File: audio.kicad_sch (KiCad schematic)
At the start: 46 parts, among them J10 NCJ6FA-H-0, J9 NCJ6FA-H-0, Q2 2N3904, Q3 2N3904, Q4 2N3906, Q5 2N3906, U10 OPA1656ID, U11 LM2903, U8 THAT1246, U9 THAT1246

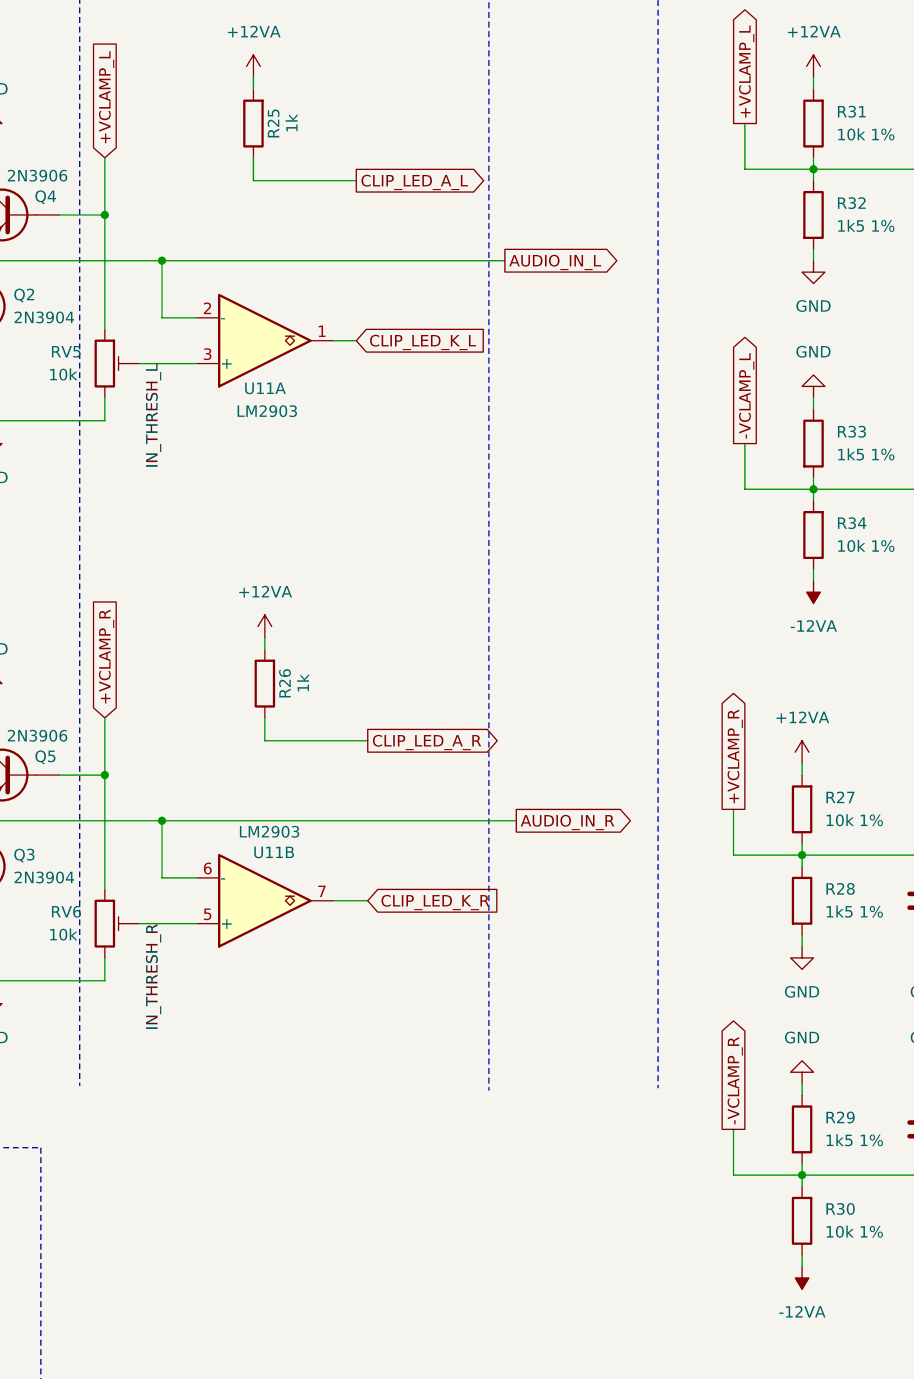
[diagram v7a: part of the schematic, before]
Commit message: introduce daughter board
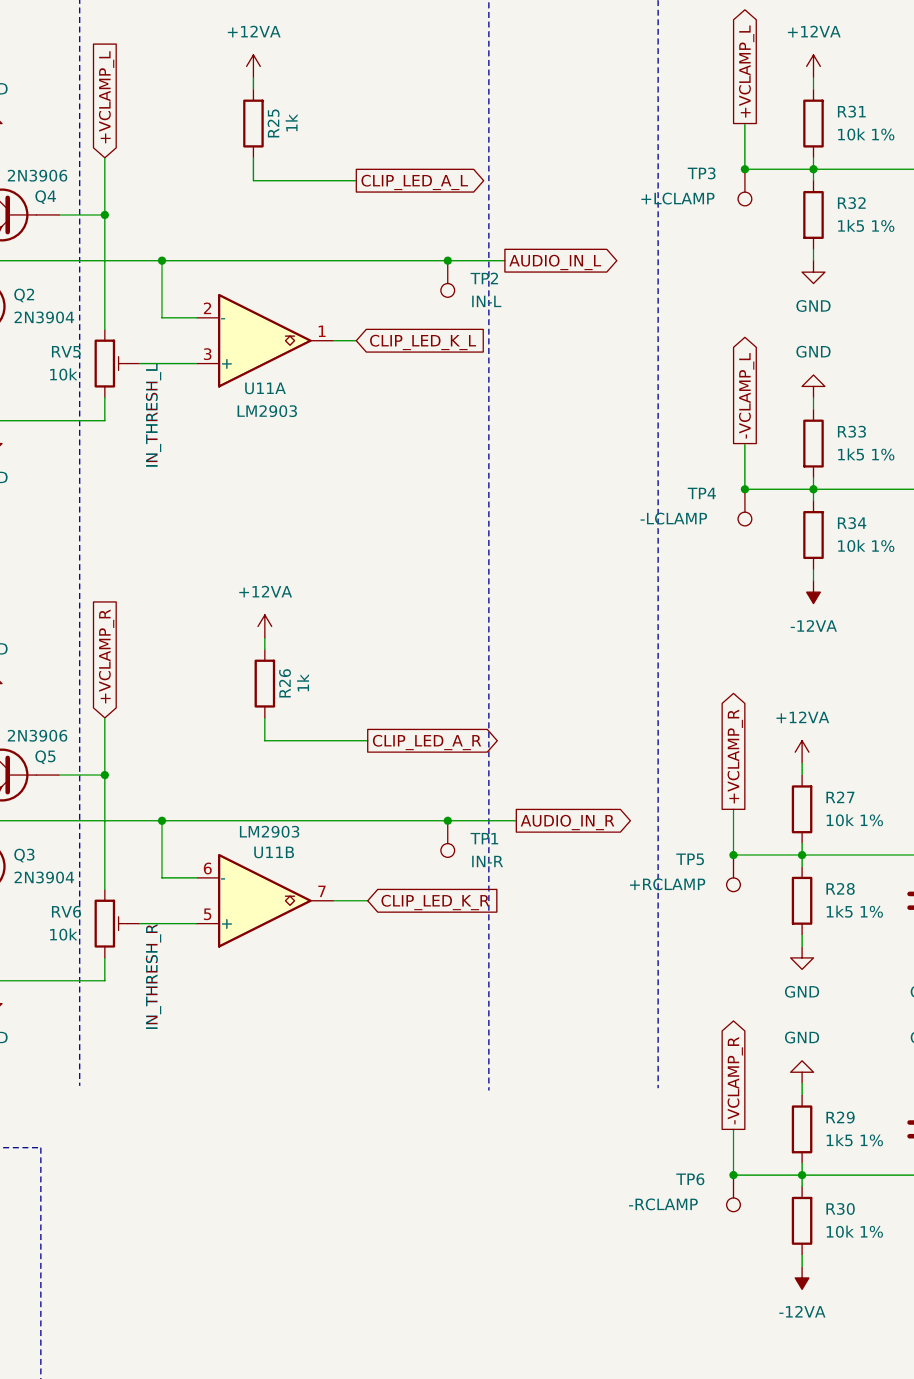
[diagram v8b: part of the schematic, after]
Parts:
- added TP1: IN-R, symbol Connector:TestPoint
- added TP2: IN-L, symbol Connector:TestPoint
- added TP3: +LCLAMP, symbol Connector:TestPoint
- added TP4: -LCLAMP, symbol Connector:TestPoint
- added TP5: +RCLAMP, symbol Connector:TestPoint
- added TP6: -RCLAMP, symbol Connector:TestPoint
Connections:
- net +VCLAMP_L: now also TP3.1
- net +VCLAMP_R: now also TP5.1
- net -VCLAMP_L: now also TP4.1
- net -VCLAMP_R: now also TP6.1
- net AUDIO_IN_L: now also TP2.1
- net AUDIO_IN_R: now also TP1.1
